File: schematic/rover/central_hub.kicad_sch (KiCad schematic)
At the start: 10 parts, among them Q1 BC547, U1 Pico

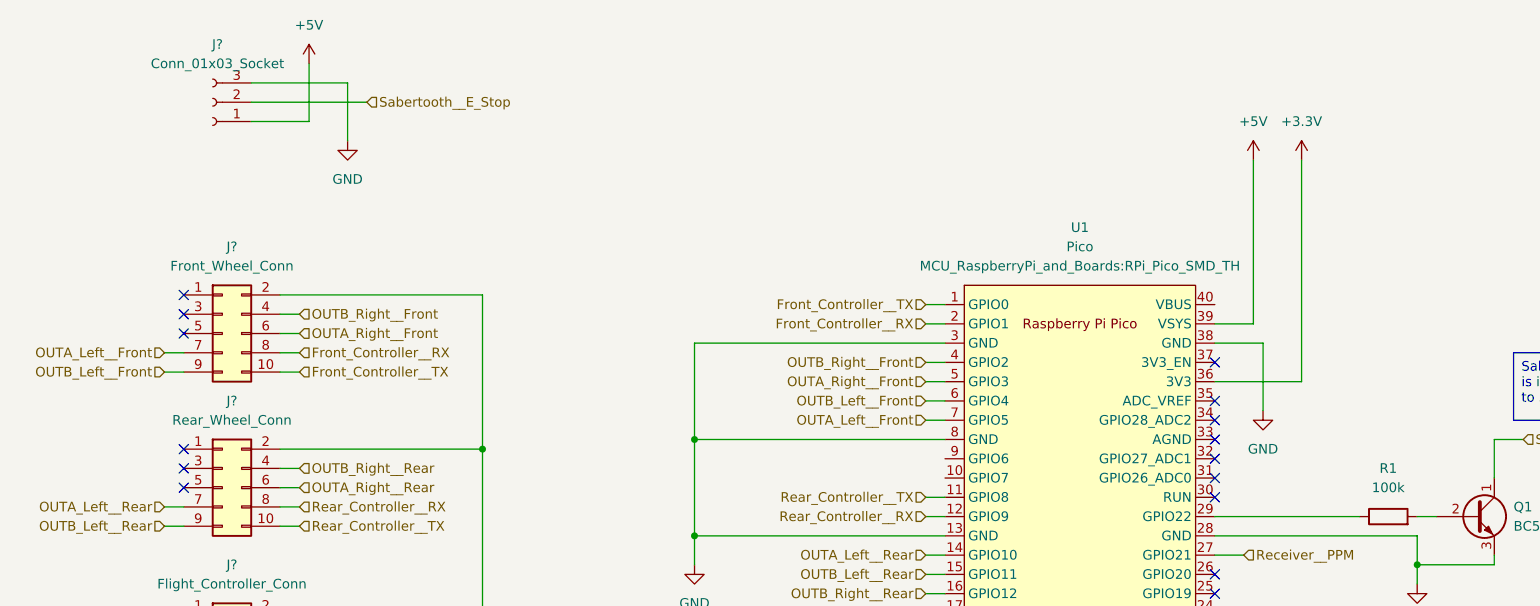
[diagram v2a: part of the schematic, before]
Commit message: Arrange components following the stripboard layout
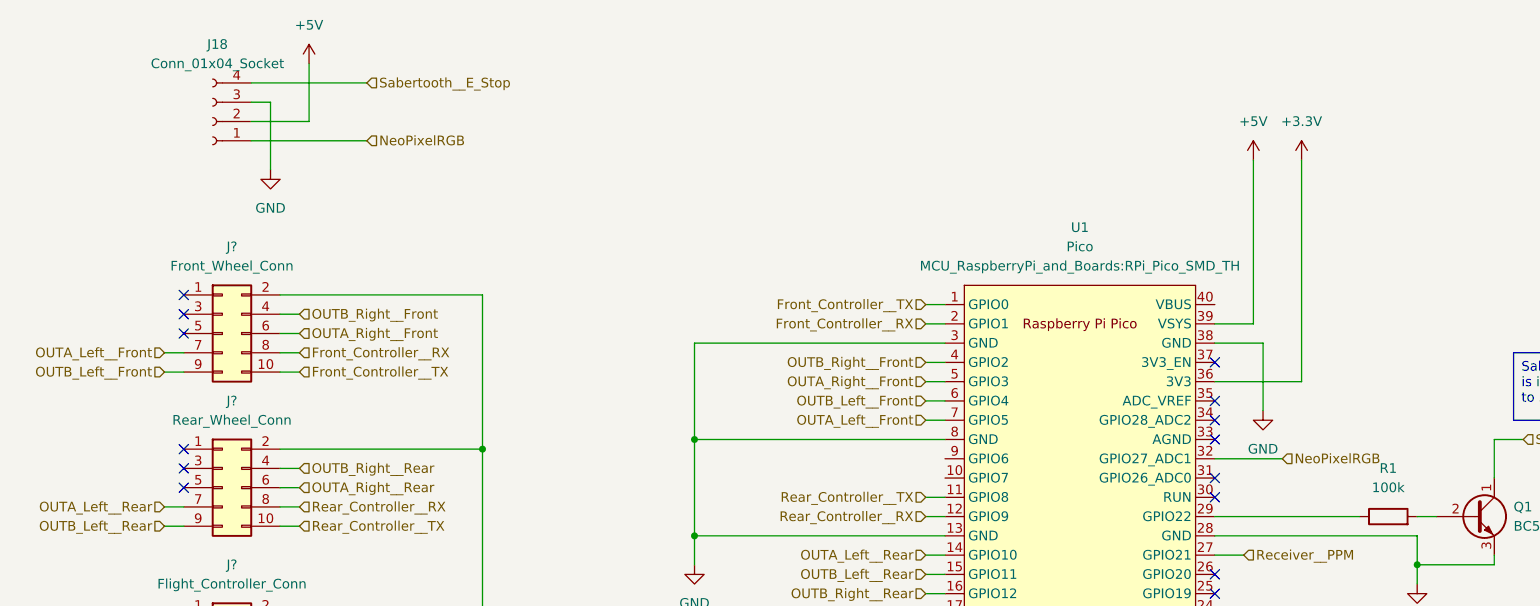
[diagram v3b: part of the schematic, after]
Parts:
- removed J?: Conn_01x03_Socket, Connector_PinHeader_2.54mm:PinHeader_1x03_P2.54mm_Vertical, symbol Connector:Conn_01x03_Socket
- added J18: Conn_01x04_Socket, Connector_PinHeader_2.54mm:PinHeader_1x04_P2.54mm_Vertical, symbol Connector:Conn_01x04_Socket
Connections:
- net +5V: now also J18.2 (Pin_2)
- net GND: now also J18.3 (Pin_3)
- net Sabertooth__E_Stop: now also J18.4 (Pin_4)
- net NeoPixelRGB: now reaches U1.32 (GPIO27_ADC1)
- net NeoPixelRGB: now also J18.1 (Pin_1)
- no-connect marks 23 -> 22
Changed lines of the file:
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@@
   (no_connect (at 251.46 114.3))
   (no_connect (at 238.76 111.76))
-  (no_connect (at 177.8 82.55))
   (no_connect (at 238.76 114.3))
   (no_connect (at 41.91 86.36))
@@
     (stroke (width 0) (type default))
   )
-  (wire (pts (xy 63.5 33.02) (xy 63.5 40.64))
-    (stroke (width 0) (type default))
-  )
   (wire (pts (xy 57.15 63.5) (xy 54.61 63.5))
     (stroke (width 0) (type default))
   )
-  (wire (pts (xy 58.42 38.1) (xy 50.8 38.1))
+  (wire (pts (xy 50.8 40.64) (xy 66.04 40.64))
     (stroke (width 0) (type default))
   )
@@
     (stroke (width 0) (type default))
   )
+  (wire (pts (xy 50.8 35.56) (xy 53.34 35.56))
+    (stroke (width 0) (type default))
+  )
   (wire (pts (xy 218.44 80.01) (xy 214.63 80.01))
     (stroke (width 0) (type default))
@@
     (stroke (width 0) (type default))
   )
-  (wire (pts (xy 50.8 33.02) (xy 63.5 33.02))
+  (wire (pts (xy 177.8 82.55) (xy 186.69 82.55))
     (stroke (width 0) (type default))
   )
@@
     (stroke (width 0) (type default))
   )
+  (wire (pts (xy 50.8 33.02) (xy 66.04 33.02))
+    (stroke (width 0) (type default))
+  )
   (wire (pts (xy 177.8 105.41) (xy 184.15 105.41))
     (stroke (width 0) (type default))
   )
-  (wire (pts (xy 66.04 35.56) (xy 50.8 35.56))
-    (stroke (width 0) (type default))
-  )
   (wire (pts (xy 54.61 60.96) (xy 81.28 60.96))
     (stroke (width 0) (type default))
@@
     (stroke (width 0) (type default))
   )
+  (wire (pts (xy 53.34 35.56) (xy 53.34 44.45))
+    (stroke (width 0) (type default))
+  )
   (wire (pts (xy 184.15 105.41) (xy 184.15 135.89))
     (stroke (width 0) (type default))
@@
   )
   (wire (pts (xy 142.24 107.95) (xy 127 107.95))
+    (stroke (width 0) (type default))
+  )
+  (wire (pts (xy 50.8 38.1) (xy 58.42 38.1))
     (stroke (width 0) (type default))
   )
@@
     (effects (font (size 1.27 1.27)) (justify left))
   )
+  (hierarchical_label "NeoPixelRGB" (shape input) (at 186.69 82.55 0) (fields_autoplaced)
+    (effects (font (size 1.27 1.27)) (justify left))
+  )
+  (hierarchical_label "NeoPixelRGB" (shape input) (at 66.04 40.64 0) (fields_autoplaced)
+    (effects (font (size 1.27 1.27)) (justify left))
+  )
   (hierarchical_label "OUTA_Left__Rear" (shape input) (at 39.37 88.9 180) (fields_autoplaced)
     (effects (font (size 1.27 1.27)) (justify right))
@@
     (effects (font (size 1.27 1.27)) (justify right))
   )
-  (hierarchical_label "Sabertooth__E_Stop" (shape input) (at 66.04 35.56 0) (fields_autoplaced)
+  (hierarchical_label "Sabertooth__E_Stop" (shape input) (at 66.04 33.02 0) (fields_autoplaced)
     (effects (font (size 1.27 1.27)) (justify left))
   )
@@
     )
   )
-  (symbol (lib_id "power:GND") (at 63.5 40.64 0) (unit 1)
-    (in_bom yes) (on_board yes) (dnp no) (fields_autoplaced)
-    (property "Reference" "#PWR?" (at 63.5 46.99 0)
-      (effects (font (size 1.27 1.27)) hide)
-    )
-    (property "Value" "GND" (at 63.5 45.72 0)
-      (effects (font (size 1.27 1.27)))
-    )
-    (property "Footprint" "" (at 63.5 40.64 0)
-      (effects (font (size 1.27 1.27)) hide)
-    )
-    (property "Datasheet" "" (at 63.5 40.64 0)
+  (symbol (lib_id "power:GND") (at 53.34 44.45 0) (unit 1)
+    (in_bom yes) (on_board yes) (dnp no) (fields_autoplaced)
+    (property "Reference" "#PWR?" (at 53.34 50.8 0)
+      (effects (font (size 1.27 1.27)) hide)
+    )
+    (property "Value" "GND" (at 53.34 49.53 0)
+      (effects (font (size 1.27 1.27)))
+    )
+    (property "Footprint" "" (at 53.34 44.45 0)
+      (effects (font (size 1.27 1.27)) hide)
+    )
+    (property "Datasheet" "" (at 53.34 44.45 0)
       (effects (font (size 1.27 1.27)) hide)
     )
@@
         (path "/e69e2e1e-a9af-4127-a558-2cc8fb636c94/8350866f-b296-4194-b8e5-2cec92f34e35/e9c65542-b8c8-4c65-8fa9-1039ffc51836"
           (reference "R1") (unit 1)
-        )
-      )
-    )
-  )
-  (symbol (lib_id "Connector:Conn_01x03_Socket") (at 45.72 35.56 180) (unit 1)
-    (in_bom yes) (on_board yes) (dnp no) (fields_autoplaced)
-    (property "Reference" "J?" (at 46.355 27.94 0)
-      (effects (font (size 1.27 1.27)))
-    )
-    (property "Value" "Conn_01x03_Socket" (at 46.355 30.48 0)
-      (effects (font (size 1.27 1.27)))
-    )
-    (property "Footprint" "Connector_PinHeader_2.54mm:PinHeader_1x03_P2.54mm_Vertical" (at 45.72 35.56 0)
-      (effects (font (size 1.27 1.27)) hide)
-    )
-    (property "Datasheet" "~" (at 45.72 35.56 0)
-      (effects (font (size 1.27 1.27)) hide)
-    )
-    (pin "3")
-    (pin "2")
-    (pin "1")
-    (instances
-      (project "rover"
-        (path "/e69e2e1e-a9af-4127-a558-2cc8fb636c94"
-          (reference "J?") (unit 1)
-        )
-        (path "/e69e2e1e-a9af-4127-a558-2cc8fb636c94/8350866f-b296-4194-b8e5-2cec92f34e35/e9c65542-b8c8-4c65-8fa9-1039ffc51836"
-          (reference "J4") (unit 1)
         )
       )
@@
         )
       )
+    )
+  )
+  (symbol (lib_id "Connector:Conn_01x04_Socket") (at 45.72 38.1 180) (unit 1)
+    (in_bom yes) (on_board yes) (dnp no) (fields_autoplaced)
+    (property "Reference" "J18" (at 46.355 27.94 0)
+      (effects (font (size 1.27 1.27)))
+    )
+    (property "Value" "Conn_01x04_Socket" (at 46.355 30.48 0)
+      (effects (font (size 1.27 1.27)))
+    )
+    (property "Footprint" "Connector_PinHeader_2.54mm:PinHeader_1x04_P2.54mm_Vertical" (at 45.72 38.1 0)
+      (effects (font (size 1.27 1.27)) hide)
+    )
+    (property "Datasheet" "~" (at 45.72 38.1 0)
+      (effects (font (size 1.27 1.27)) hide)
+    )
+    (pin "2")
+    (pin "4")
+    (pin "3")
+    (pin "1")
+    (instances
+      (project "rover"
+        (path "/e69e2e1e-a9af-4127-a558-2cc8fb636c94/8350866f-b296-4194-b8e5-2cec92f34e35/e9c65542-b8c8-4c65-8fa9-1039ffc51836"
+          (reference "J18") (unit 1)
+        )
+      )
